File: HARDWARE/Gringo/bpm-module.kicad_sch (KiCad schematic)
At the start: 21 parts, among them J17 Conn_01x05_Pin, U4 PTPS7A2018PDBVR, U5 MAX30101EFD+, U6 MAX32664GWEA+T, U7 PAM2401YPADJ, Y1 32k768

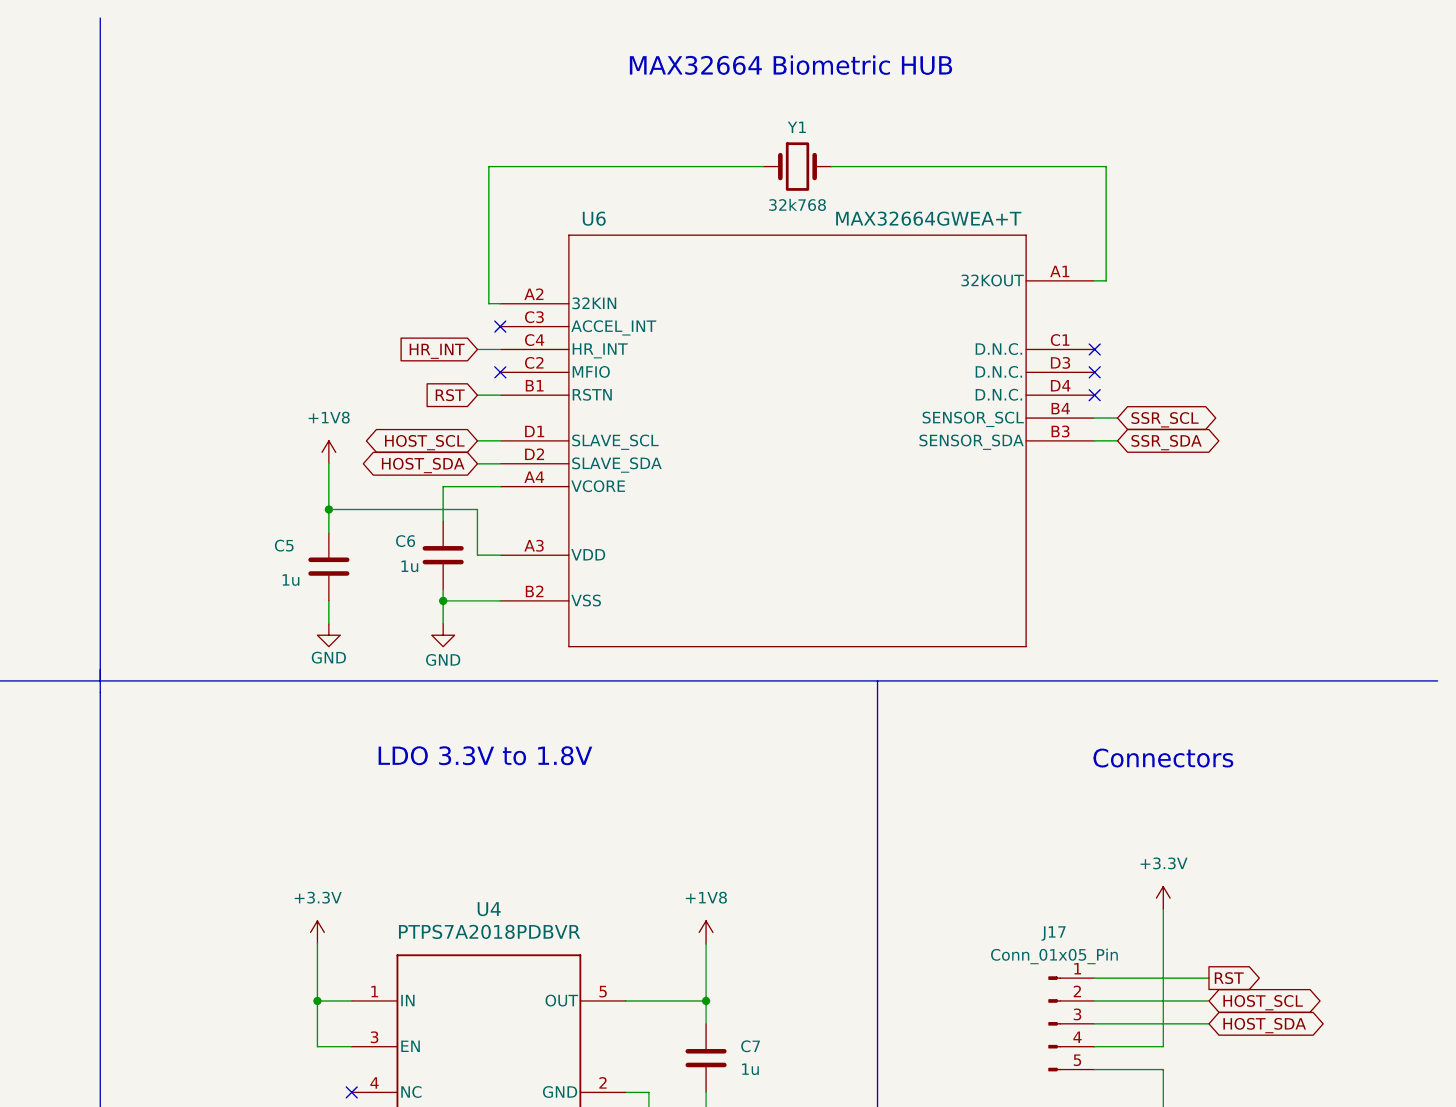
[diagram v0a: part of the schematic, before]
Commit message: Update scheme and PCB for evk boards with adapted component packages
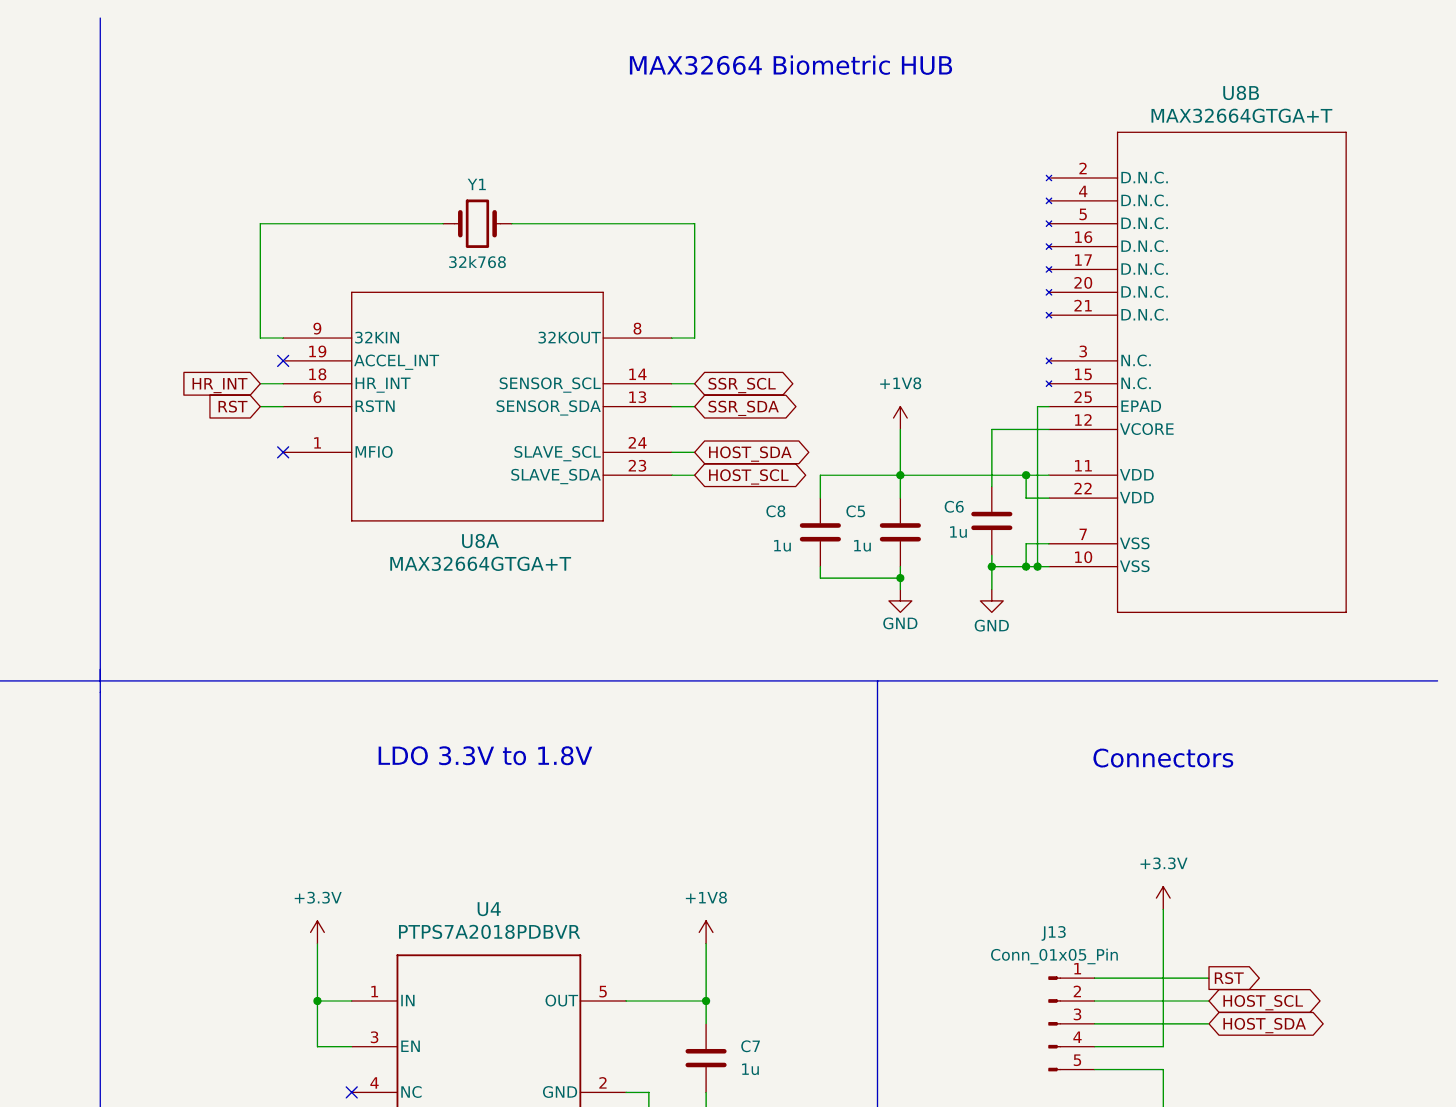
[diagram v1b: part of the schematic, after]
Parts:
- removed U6: MAX32664GWEA+T, MAX32664GWEA-T:21-100241A_W161K1&plus_1_MXM, symbol MAX32664GWEA-functionnal:MAX32664GWEA+T
- added C8: 1u, Capacitor_SMD:C_0603_1608Metric, symbol Device:C
- added U8: MAX32664GTGA+T, MAX32664GTGA-T:21-100264_T2433&plus_2C_MXM, symbol MAX32664GTGA-T:MAX32664GTGA+T
- U5: footprint MAX30101EFD:21-1048_F143A5&plus_1_MXM-M -> MAX30101EFD-:21-1048_F143A5&plus_1_MXM
- renumbered J17 to J13
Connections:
- net +1V8: now also C8.1, U8.11 (VDD), U8.22 (VDD)
- net GND: now also C8.2, U8.10 (VSS), U8.25 (EPAD), U8.7 (VSS)
- net HOST_SCL: now also U8.23 (SLAVE_SDA)
- net HOST_SDA: now also U8.24 (SLAVE_SCL)
- net HR_INT: now also U8.18 (HR_INT)
- net RST: now also U8.6 (RSTN)
- net SSR_SCL: now also U8.14 (SENSOR_SCL)
- net SSR_SDA: now also U8.13 (SENSOR_SDA)
- net at Y1.2: now also U8.8 (32KOUT)
- net at Y1.1: now also U8.9 (32KIN)
- net at C6.1: now also U8.12 (VCORE)
- no-connect marks 15 -> 12

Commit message: Update inductor package
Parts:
- L1: footprint Inductor_SMD:L_0603_1608Metric -> Inductor_SMD:L_APV_ANR4030
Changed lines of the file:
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@@
 			)
 		)
-		(property "Footprint" "Inductor_SMD:L_0603_1608Metric"
+		(property "Footprint" "Inductor_SMD:L_APV_ANR4030"
 			(at 43.18 134.62 0)
 			(effects

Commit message: Update the quartz model
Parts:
- Y1: footprint Crystal:Crystal_SMD_2012-2Pin_2.0x1.2mm -> ECS-327-12-5-12-TR:XTAL_ECX-12_2X1P2_ECS
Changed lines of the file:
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@@
 			)
 		)
-		(property "Footprint" "Crystal:Crystal_SMD_2012-2Pin_2.0x1.2mm"
+		(property "Footprint" "ECS-327-12-5-12-TR:XTAL_ECX-12_2X1P2_ECS"
 			(at 177.8 35.56 0)
 			(effects
